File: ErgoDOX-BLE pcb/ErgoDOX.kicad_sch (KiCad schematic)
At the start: 99 parts, among them J1 Conn_01x04, J2 Conn_01x02_Female, J3 Conn_01x02_Female, J4 Conn_01x02, J5 Conn_01x02, J6 6PIN, P1 USB_C_Plug_USB2.0, Q1 Q_NPN_BCE, SW0:10 SW0:3, SW0:11 SW0:2, SW0:12 SW0:1, SW0:7 SW0:6, SW0:8 SW0:5, SW0:9 SW0:4, SW1:10 SW1:3, SW1:11 SW1:2, SW1:12 SW1:1, SW1:13 SW1:0, SW1:9 SW1:4, SW2:10 SW2:3, SW2:11 SW2:2, SW2:12 SW2:1, SW2:13 SW2:0, SW2:7 SW2:6, SW2:8 SW2:5, SW2:9 SW2:4, SW3:10 SW3:3, SW3:11 SW3:2, SW3:12 SW3:1, SW3:13 SW3:0, SW3:8 SW3:5, SW3:9 SW3:4, SW4:10 SW4:3, SW4:11 SW4:2, SW4:12 SW4:1, SW4:13 SW4:0, SW4:7 SW4:6, SW4:8 SW4:5, SW4:9 SW4:4, SW5:10 SW5:3, SW5:11 SW5:2, SW5:12 SW5:1, SW5:13 SW5:0, SW5:7 SW5:6, SW5:8 SW5:5, SW5:9 SW5:4, U1 MCP23018

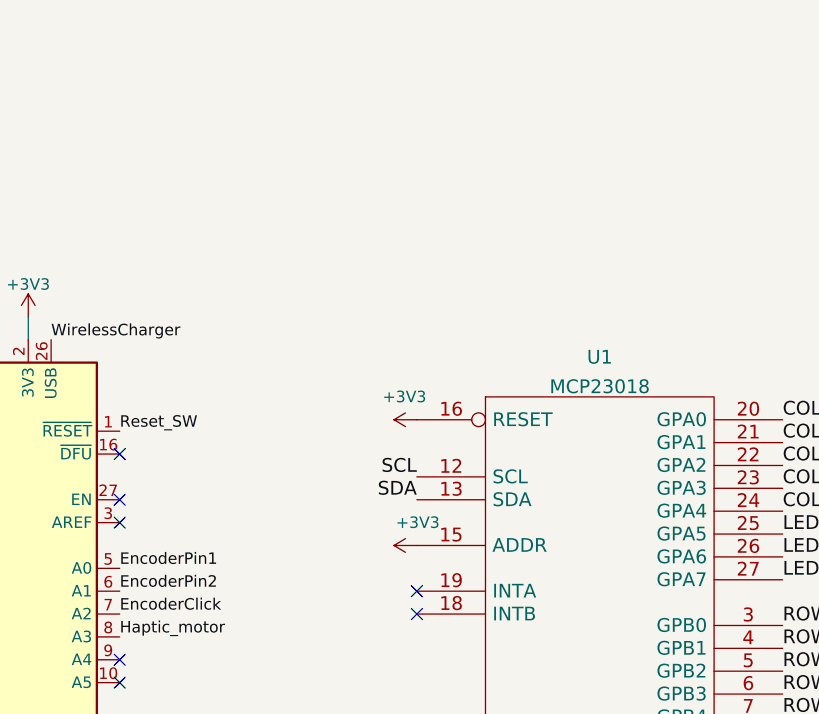
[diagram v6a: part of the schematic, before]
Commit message: Add jumpers for setting address of IO expander
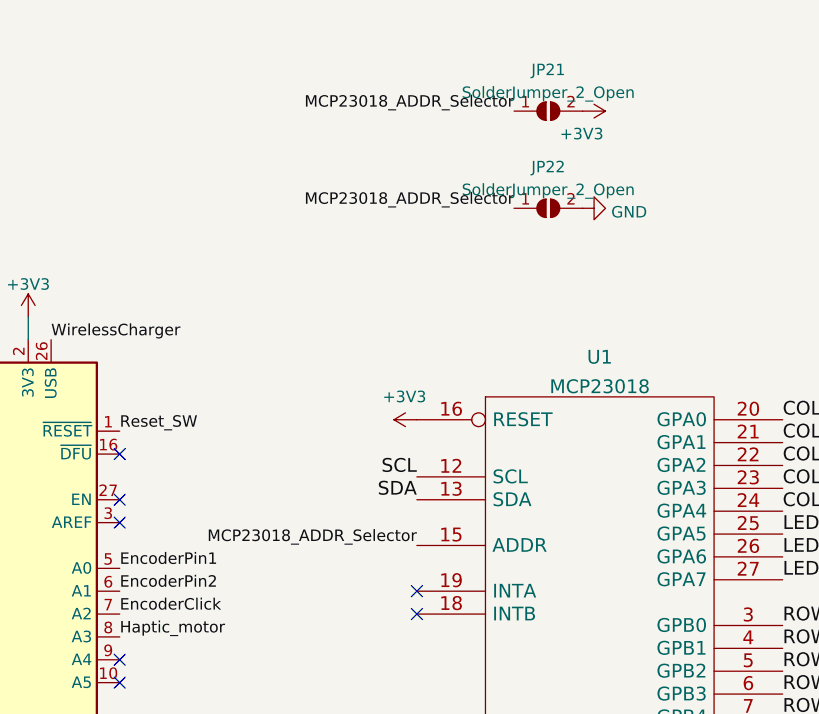
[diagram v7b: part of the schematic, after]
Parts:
- added JP21, JP22: SolderJumper_2_Open, Jumper:SolderJumper-2_P1.3mm_Open_RoundedPad1.0x1.5mm, symbol Jumper:SolderJumper_2_Open
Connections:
- net +3V3: now also JP21.2 (B); no longer U1.15 (ADDR)
- net GND: now also JP22.2 (B)
- new net MCP23018_ADDR_Selector: JP21.1 (A), JP22.1 (A), U1.15 (ADDR)
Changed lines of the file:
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@@
+    (effects (font (size 1.27 1.27)) (justify right bottom))
+  )
+  (label "MCP23018_ADDR_Selector" (at 310.515 33.655 180)
     (effects (font (size 1.27 1.27)) (justify right bottom))
   )
@@
     (effects (font (size 1.27 1.27)) (justify left bottom))
   )
+  (label "MCP23018_ADDR_Selector" (at 299.72 71.12 180)
+    (effects (font (size 1.27 1.27)) (justify right bottom))
+  )
   (label "ROW3" (at 340.36 85.09 0)
     (effects (font (size 1.524 1.524)) (justify left bottom))
@@
   (label "SDA" (at 299.72 66.04 180)
     (effects (font (size 1.524 1.524)) (justify right bottom))
+  )
+  (label "MCP23018_ADDR_Selector" (at 310.515 22.86 180)
+    (effects (font (size 1.27 1.27)) (justify right bottom))
   )
   (label "SDA" (at 311.785 237.49 0)
@@
     (pin "2")
   )
+  (symbol (lib_id "Jumper:SolderJumper_2_Open") (at 314.325 22.86 0) (unit 1)
+    (in_bom yes) (on_board yes) (fields_autoplaced)
+    (property "Reference" "JP21" (id 0) (at 314.325 18.2712 0))
+    (property "Value" "SolderJumper_2_Open" (id 1) (at 314.325 20.8081 0))
+    (property "Footprint" "Jumper:SolderJumper-2_P1.3mm_Open_RoundedPad1.0x1.5mm" (id 2) (at 314.325 22.86 0)
+      (effects (font (size 1.27 1.27)) hide)
+    )
+    (property "Datasheet" "~" (id 3) (at 314.325 22.86 0)
+      (effects (font (size 1.27 1.27)) hide)
+    )
+    (pin "1")
+    (pin "2")
+  )
   (symbol (lib_id "power:+3V3") (at 361.95 238.125 270) (unit 1)
     (in_bom yes) (on_board yes)
@@
     (pin "2")
   )
+  (symbol (lib_id "Jumper:SolderJumper_2_Open") (at 314.325 33.655 0) (unit 1)
+    (in_bom yes) (on_board yes) (fields_autoplaced)
+    (property "Reference" "JP22" (id 0) (at 314.325 29.0662 0))
+    (property "Value" "SolderJumper_2_Open" (id 1) (at 314.325 31.6031 0))
+    (property "Footprint" "Jumper:SolderJumper-2_P1.3mm_Open_RoundedPad1.0x1.5mm" (id 2) (at 314.325 33.655 0)
+      (effects (font (size 1.27 1.27)) hide)
+    )
+    (property "Datasheet" "~" (id 3) (at 314.325 33.655 0)
+      (effects (font (size 1.27 1.27)) hide)
+    )
+    (pin "1")
+    (pin "2")
+  )
   (symbol (lib_id "component:6PIN") (at 245.11 250.19 0) (unit 1)
     (in_bom yes) (on_board yes) (fields_autoplaced)
@@
     (pin "4")
   )
-  (symbol (lib_id "power:+3V3") (at 299.72 71.12 90) (unit 1)
-    (in_bom yes) (on_board yes)
-    (property "Reference" "#PWR029" (id 0) (at 303.53 71.12 0)
-      (effects (font (size 1.27 1.27)) hide)
-    )
-    (property "Value" "+3V3" (id 1) (at 302.26 68.58 90)
+  (symbol (lib_id "power:+3V3") (at 318.135 22.86 270) (unit 1)
+    (in_bom yes) (on_board yes)
+    (property "Reference" "#PWR029" (id 0) (at 314.325 22.86 0)
+      (effects (font (size 1.27 1.27)) hide)
+    )
+    (property "Value" "+3V3" (id 1) (at 315.595 25.4 90)
       (effects (font (size 1.27 1.27)) (justify left))
     )
-    (property "Footprint" "" (id 2) (at 299.72 71.12 0)
-      (effects (font (size 1.27 1.27)) hide)
-    )
-    (property "Datasheet" "" (id 3) (at 299.72 71.12 0)
+    (property "Footprint" "" (id 2) (at 318.135 22.86 0)
+      (effects (font (size 1.27 1.27)) hide)
+    )
+    (property "Datasheet" "" (id 3) (at 318.135 22.86 0)
       (effects (font (size 1.27 1.27)) hide)
     )
@@
     )
     (property "Datasheet" "" (id 3) (at 207.645 216.535 0)
+      (effects (font (size 1.27 1.27)) hide)
+    )
+    (pin "1")
+  )
+  (symbol (lib_id "power:GND") (at 318.135 33.655 90) (unit 1)
+    (in_bom yes) (on_board yes) (fields_autoplaced)
+    (property "Reference" "#PWR027" (id 0) (at 324.485 33.655 0)
+      (effects (font (size 1.27 1.27)) hide)
+    )
+    (property "Value" "GND" (id 1) (at 321.31 34.0888 90)
+      (effects (font (size 1.27 1.27)) (justify right))
+    )
+    (property "Footprint" "" (id 2) (at 318.135 33.655 0)
+      (effects (font (size 1.27 1.27)) hide)
+    )
+    (property "Datasheet" "" (id 3) (at 318.135 33.655 0)
       (effects (font (size 1.27 1.27)) hide)
     )
@@
       (reference "#PWR026") (unit 1) (value "+3V3") (footprint "")
     )
+    (path "/e700ad51-9fac-44e0-95e1-660846440c94"
+      (reference "#PWR027") (unit 1) (value "GND") (footprint "")
+    )
     (path "/e0d78f56-637c-46d4-adb7-54ec9ed9a717"
       (reference "#PWR028") (unit 1) (value "+3V3") (footprint "")
@@
       (reference "JP20") (unit 1) (value "SolderJumper_2_Open") (footprint "Jumper:SolderJumper-2_P1.3mm_Open_RoundedPad1.0x1.5mm")
     )
+    (path "/730a5e84-faf3-43bf-aefb-2e230e9339e3"
+      (reference "JP21") (unit 1) (value "SolderJumper_2_Open") (footprint "Jumper:SolderJumper-2_P1.3mm_Open_RoundedPad1.0x1.5mm")
+    )
+    (path "/bdc93056-fd61-48d1-9a1f-ee20680f3b06"
+      (reference "JP22") (unit 1) (value "SolderJumper_2_Open") (footprint "Jumper:SolderJumper-2_P1.3mm_Open_RoundedPad1.0x1.5mm")
+    )
     (path "/00000000-0000-0000-0000-00004f64e802"

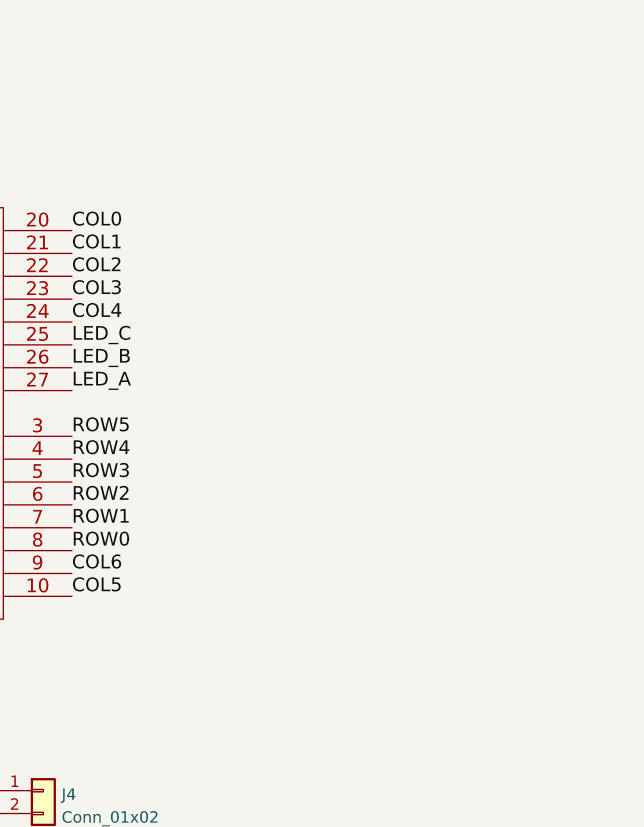
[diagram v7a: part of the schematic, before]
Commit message: Begin playing around with replacing the 23018 with a 23017
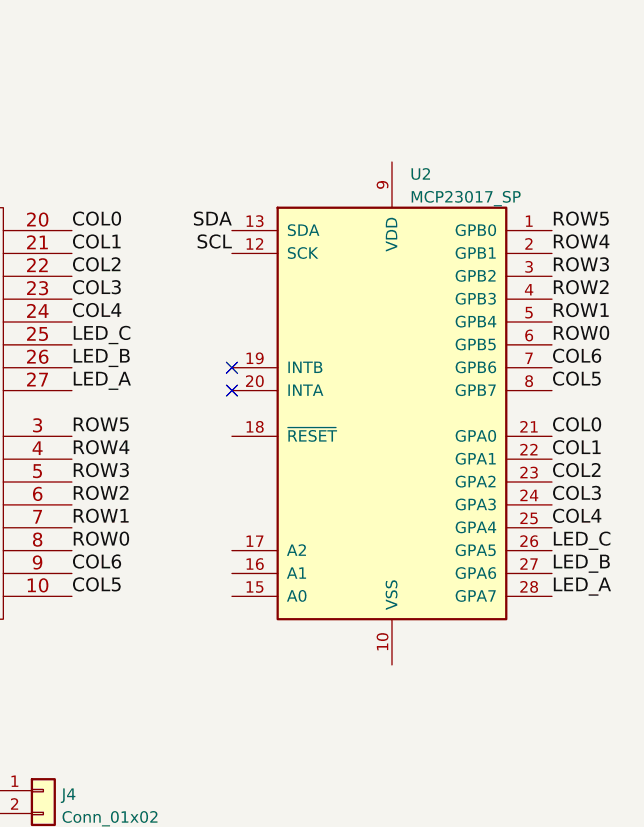
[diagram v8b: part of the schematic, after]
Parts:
- added U2: MCP23017_SP, Package_DIP:DIP-28_W7.62mm, symbol Interface_Expansion:MCP23017_SP
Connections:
- net COL0: now also U2.21 (GPA0)
- net COL1: now also U2.22 (GPA1)
- net COL2: now also U2.23 (GPA2)
- net COL3: now also U2.24 (GPA3)
- net COL4: now also U2.25 (GPA4)
- net COL5: now also U2.8 (GPB7)
- net COL6: now also U2.7 (GPB6)
- net LED_A: now also U2.28 (GPA7)
- net LED_B: now also U2.27 (GPA6)
- net LED_C: now also U2.26 (GPA5)
- net ROW0: now also U2.6 (GPB5)
- net ROW1: now also U2.5 (GPB4)
- net ROW2: now also U2.4 (GPB3)
- net ROW3: now also U2.3 (GPB2)
- net ROW4: now also U2.2 (GPB1)
- net ROW5: now also U2.1 (GPB0)
- net SCL: now also U2.12 (SCK)
- net SDA: now also U2.13 (SDA)
- no-connect marks 38 -> 40
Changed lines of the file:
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@@
   (no_connect (at 266.7 86.36))
   (no_connect (at 266.7 83.82))
+  (no_connect (at 358.14 74.93))
   (no_connect (at 133.35 76.835))
   (no_connect (at 158.75 58.42))
   (no_connect (at 133.35 73.66))
+  (no_connect (at 358.14 72.39))
   (no_connect (at 133.35 48.26))
   (no_connect (at 133.35 71.12))
@@
     (effects (font (size 1.524 1.524)) (justify left bottom))
   )
+  (label "COL4" (at 393.7 90.17 0)
+    (effects (font (size 1.524 1.524)) (justify left bottom))
+  )
   (label "D+" (at 199.39 139.7 180)
     (effects (font (size 1.27 1.27)) (justify right bottom))
@@
     (effects (font (size 1.27 1.27)) (justify right bottom))
   )
+  (label "LED_C" (at 393.7 92.71 0)
+    (effects (font (size 1.524 1.524)) (justify left bottom))
+  )
   (label "OLED_P3" (at 354.33 238.125 180)
     (effects (font (size 1.27 1.27)) (justify right bottom))
   )
+  (label "COL5" (at 393.7 74.93 0)
+    (effects (font (size 1.524 1.524)) (justify left bottom))
+  )
   (label "SDA" (at 133.35 88.9 180)
     (effects (font (size 1.524 1.524)) (justify right bottom))
@@
     (effects (font (size 1.524 1.524)) (justify left bottom))
   )
+  (label "COL0" (at 393.7 80.01 0)
+    (effects (font (size 1.524 1.524)) (justify left bottom))
+  )
   (label "SCL" (at 241.3 101.6 180)
     (effects (font (size 1.524 1.524)) (justify right bottom))
@@
     (effects (font (size 1.524 1.524)) (justify right bottom))
   )
+  (label "ROW3" (at 393.7 62.23 0)
+    (effects (font (size 1.524 1.524)) (justify left bottom))
+  )
   (label "SDA" (at 250.19 246.38 0)
     (effects (font (size 1.524 1.524)) (justify left bottom))
@@
     (effects (font (size 1.27 1.27)) (justify right bottom))
   )
+  (label "LED_A" (at 393.7 97.79 0)
+    (effects (font (size 1.524 1.524)) (justify left bottom))
+  )
   (label "Reset_SW" (at 266.7 58.42 0)
     (effects (font (size 1.27 1.27)) (justify left bottom))
@@
     (effects (font (size 1.27 1.27)) (justify right bottom))
   )
+  (label "COL2" (at 393.7 85.09 0)
+    (effects (font (size 1.524 1.524)) (justify left bottom))
+  )
   (label "OLED_P4" (at 250.19 251.46 0)
     (effects (font (size 1.27 1.27)) (justify left bottom))
   )
+  (label "ROW1" (at 393.7 67.31 0)
+    (effects (font (size 1.524 1.524)) (justify left bottom))
+  )
+  (label "ROW0" (at 393.7 69.85 0)
+    (effects (font (size 1.524 1.524)) (justify left bottom))
+  )
+  (label "SDA" (at 358.14 57.15 180)
+    (effects (font (size 1.524 1.524)) (justify right bottom))
+  )
   (label "MCP23018_ADDR_Selector" (at 299.72 71.12 180)
     (effects (font (size 1.27 1.27)) (justify right bottom))
@@
     (effects (font (size 1.524 1.524)) (justify right bottom))
   )
+  (label "ROW5" (at 393.7 57.15 0)
+    (effects (font (size 1.524 1.524)) (justify left bottom))
+  )
   (label "WirelessCharger" (at 307.975 119.38 180)
     (effects (font (size 1.27 1.27)) (justify right bottom))
@@
     (effects (font (size 1.27 1.27)) (justify right bottom))
   )
+  (label "COL3" (at 393.7 87.63 0)
+    (effects (font (size 1.524 1.524)) (justify left bottom))
+  )
   (label "Underglow DIN" (at 178.435 208.28 0)
     (effects (font (size 1.27 1.27)) (justify left bottom))
@@
     (effects (font (size 1.524 1.524)) (justify left bottom))
   )
+  (label "SCL" (at 358.14 59.69 180)
+    (effects (font (size 1.524 1.524)) (justify right bottom))
+  )
   (label "OLED_P1" (at 304.165 237.49 180)
     (effects (font (size 1.27 1.27)) (justify right bottom))
@@
     (effects (font (size 1.27 1.27)) (justify left bottom))
   )
+  (label "COL1" (at 393.7 82.55 0)
+    (effects (font (size 1.524 1.524)) (justify left bottom))
+  )
   (label "COL5" (at 60.96 250.19 270)
     (effects (font (size 1.524 1.524)) (justify right bottom))
@@
     (effects (font (size 1.27 1.27)) (justify left bottom))
   )
+  (label "ROW4" (at 393.7 59.69 0)
+    (effects (font (size 1.524 1.524)) (justify left bottom))
+  )
   (label "LED_C" (at 49.53 50.8 0)
     (effects (font (size 1.524 1.524)) (justify left bottom))
@@
     (effects (font (size 1.524 1.524)) (justify right bottom))
   )
+  (label "ROW2" (at 393.7 64.77 0)
+    (effects (font (size 1.524 1.524)) (justify left bottom))
+  )
   (label "EncoderClick" (at 266.7 78.74 0)
     (effects (font (size 1.27 1.27)) (justify left bottom))
@@
     (effects (font (size 1.524 1.524)) (justify left bottom))
   )
+  (label "COL6" (at 393.7 72.39 0)
+    (effects (font (size 1.524 1.524)) (justify left bottom))
+  )
   (label "D_IN_RIGHT-" (at 97.79 117.475 180)
     (effects (font (size 1.27 1.27)) (justify right bottom))
@@
     (effects (font (size 1.27 1.27)) (justify right bottom))
   )
+  (label "LED_B" (at 393.7 95.25 0)
+    (effects (font (size 1.524 1.524)) (justify left bottom))
+  )
   (label "SDA" (at 241.3 99.06 180)
     (effects (font (size 1.524 1.524)) (justify right bottom))
@@
     (pin "1")
   )
+  (symbol (lib_id "Interface_Expansion:MCP23017_SP") (at 375.92 77.47 0) (unit 1)
+    (in_bom yes) (on_board yes) (fields_autoplaced)
+    (property "Reference" "U2" (id 0) (at 377.9394 50.9102 0)
+      (effects (font (size 1.27 1.27)) (justify left))
+    )
+    (property "Value" "MCP23017_SP" (id 1) (at 377.9394 53.4471 0)
+      (effects (font (size 1.27 1.27)) (justify left))
+    )
+    (property "Footprint" "Package_DIP:DIP-28_W7.62mm" (id 2) (at 381 102.87 0)
+      (effects (font (size 1.27 1.27)) (justify left) hide)
+    )
+    (property "Datasheet" "http://ww1.microchip.com/downloads/en/DeviceDoc/20001952C.pdf" (id 3) (at 381 105.41 0)
+      (effects (font (size 1.27 1.27)) (justify left) hide)
+    )
+    (pin "1")
+    (pin "10")
+    (pin "11")
+    (pin "12")
+    (pin "13")
+    (pin "14")
+    (pin "15")
+    (pin "16")
+    (pin "17")
+    (pin "18")
+    (pin "19")
+    (pin "2")
+    (pin "20")
+    (pin "21")
+    (pin "22")
+    (pin "23")
+    (pin "24")
+    (pin "25")
+    (pin "26")
+    (pin "27")
+    (pin "28")
+    (pin "3")
+    (pin "4")
+    (pin "5")
+    (pin "6")
+    (pin "7")
+    (pin "8")
+    (pin "9")
+  )
   (symbol (lib_id "component:GND") (at 313.055 247.65 90) (unit 1)
     (in_bom yes) (on_board yes) (fields_autoplaced)
@@
       (reference "U1") (unit 1) (value "MCP23018") (footprint "ErgoDOX pcb:DIP28_300")
     )
+    (path "/474dc503-d481-40df-ae5d-6d0bef31540b"
+      (reference "U2") (unit 1) (value "MCP23017_SP") (footprint "Package_DIP:DIP-28_W7.62mm")
+    )
     (path "/541ff60d-8106-419f-8b31-7003c4d8f0bd"
